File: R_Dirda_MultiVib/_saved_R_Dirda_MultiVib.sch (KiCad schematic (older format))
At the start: 11 parts

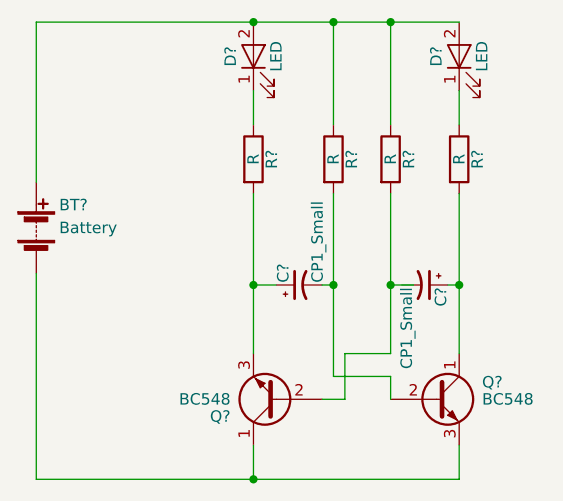
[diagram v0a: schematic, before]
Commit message: 0.2
Tranzistori BC548 tiek aizstati ar IC mikroshemu

This reverts commit 3d703b0aae8bc0295c59cc91b30c956ba27862da.
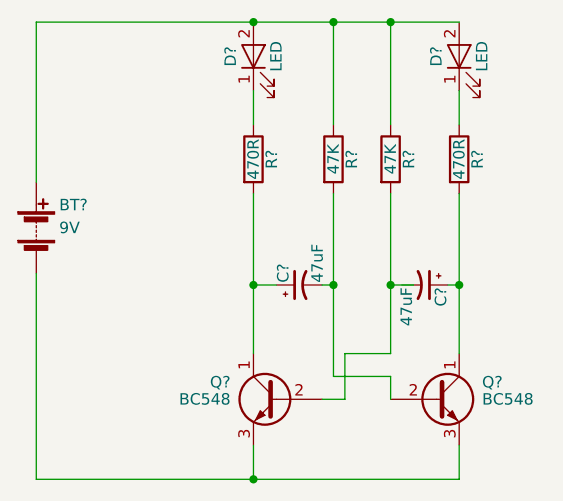
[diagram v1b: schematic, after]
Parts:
- BT?: value Battery -> 9V
- C? (x2): value CP1_Small -> 47uF
- R? (x2): value R -> 470R
- R? (x2): value R -> 47K
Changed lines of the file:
@@
 LIBS:contrib
 LIBS:valves
+LIBS:bcm586ds
+LIBS:R_Dirda_MultiVib-cache
 EELAYER 25 0
 EELAYER END
@@
 P 2650 3200
 F 0 "R?" V 2730 3200 50  0000 C CNN
-F 1 "R" V 2650 3200 50  0000 C CNN
+F 1 "470R" V 2650 3200 50  0000 C CNN
 F 2 "" V 2580 3200 50  0001 C CNN
 F 3 "" H 2650 3200 50  0001 C CNN
@@
 P 3000 3200
 F 0 "R?" V 3080 3200 50  0000 C CNN
-F 1 "R" V 3000 3200 50  0000 C CNN
+F 1 "47K" V 3000 3200 50  0000 C CNN
 F 2 "" V 2930 3200 50  0001 C CNN
 F 3 "" H 3000 3200 50  0001 C CNN
@@
 P 3250 3200
 F 0 "R?" V 3330 3200 50  0000 C CNN
-F 1 "R" V 3250 3200 50  0000 C CNN
+F 1 "47K" V 3250 3200 50  0000 C CNN
 F 2 "" V 3180 3200 50  0001 C CNN
 F 3 "" H 3250 3200 50  0001 C CNN
@@
 P 3550 3200
 F 0 "R?" V 3630 3200 50  0000 C CNN
-F 1 "R" V 3550 3200 50  0000 C CNN
+F 1 "470R" V 3550 3200 50  0000 C CNN
 F 2 "" V 3480 3200 50  0001 C CNN
 F 3 "" H 3550 3200 50  0001 C CNN
@@
 P 1700 3500
 F 0 "BT?" H 1800 3600 50  0000 L CNN
-F 1 "Battery" H 1800 3500 50  0000 L CNN
+F 1 "9V" H 1800 3500 50  0000 L CNN
 F 2 "" V 1700 3560 50  0001 C CNN
 F 3 "" V 1700 3560 50  0001 C CNN
@@
 P 2850 3750
 F 0 "C?" H 2860 3820 50  0000 L CNN
-F 1 "CP1_Small" H 2860 3670 50  0000 L CNN
+F 1 "47uF" H 2860 3670 50  0000 L CNN
 F 2 "" H 2850 3750 50  0001 C CNN
 F 3 "" H 2850 3750 50  0001 C CNN
@@
 P 3400 3750
 F 0 "C?" H 3410 3820 50  0000 L CNN
-F 1 "CP1_Small" H 3410 3670 50  0000 L CNN
+F 1 "47uF" H 3410 3670 50  0000 L CNN
 F 2 "" H 3400 3750 50  0001 C CNN
 F 3 "" H 3400 3750 50  0001 C CNN
@@
 F 3 "" H 2750 4250 50  0001 L CNN
 	1    2750 4250
-	-1   0    0    1
+	-1   0    0    -1
 $EndComp
 $Comp
